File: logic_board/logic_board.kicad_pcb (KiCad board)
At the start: 4 copper layers, 80 x 30 mm, 55 parts, among them J1 Debug, J2 Audio In, J3 SJ2-3595X-SMT, J4 Amphenol 124015, J5 Batt, SW1 TL3315NF160Q, SW2 TL3315NF160Q, SW3 TL3315NF160Q, SW4 TL3315NF160Q, SW5 Power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

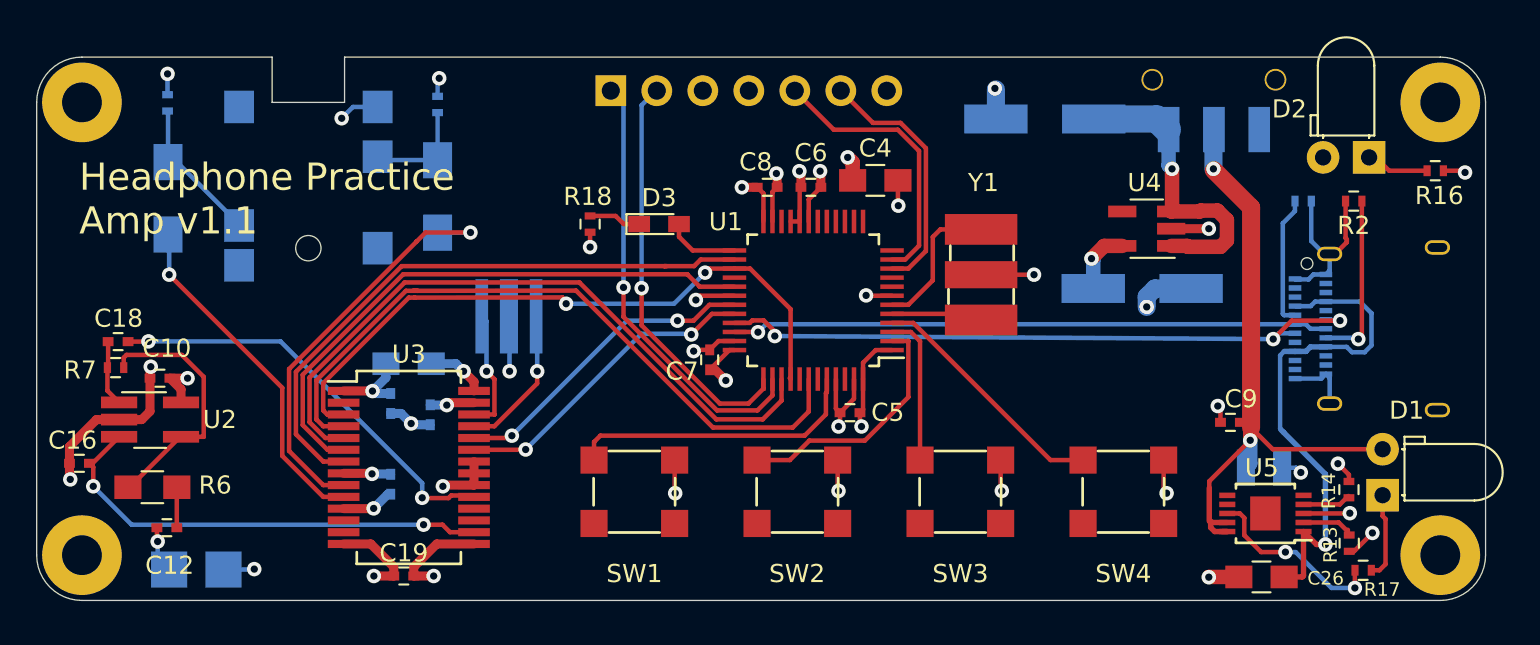
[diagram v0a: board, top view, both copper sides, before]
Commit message: Use longer screws
The M2x6 screws are too short with the PCB in place. This requires upgrading to M2.3 screws.
Increased bore sizes. I had to make the top bosses tapered to accomodate the larger counterbore.
I tapered the bottom ones just to match.
Also increased the RELIEF to 0.8, as the parts do warp a bit and things stick during assembly.
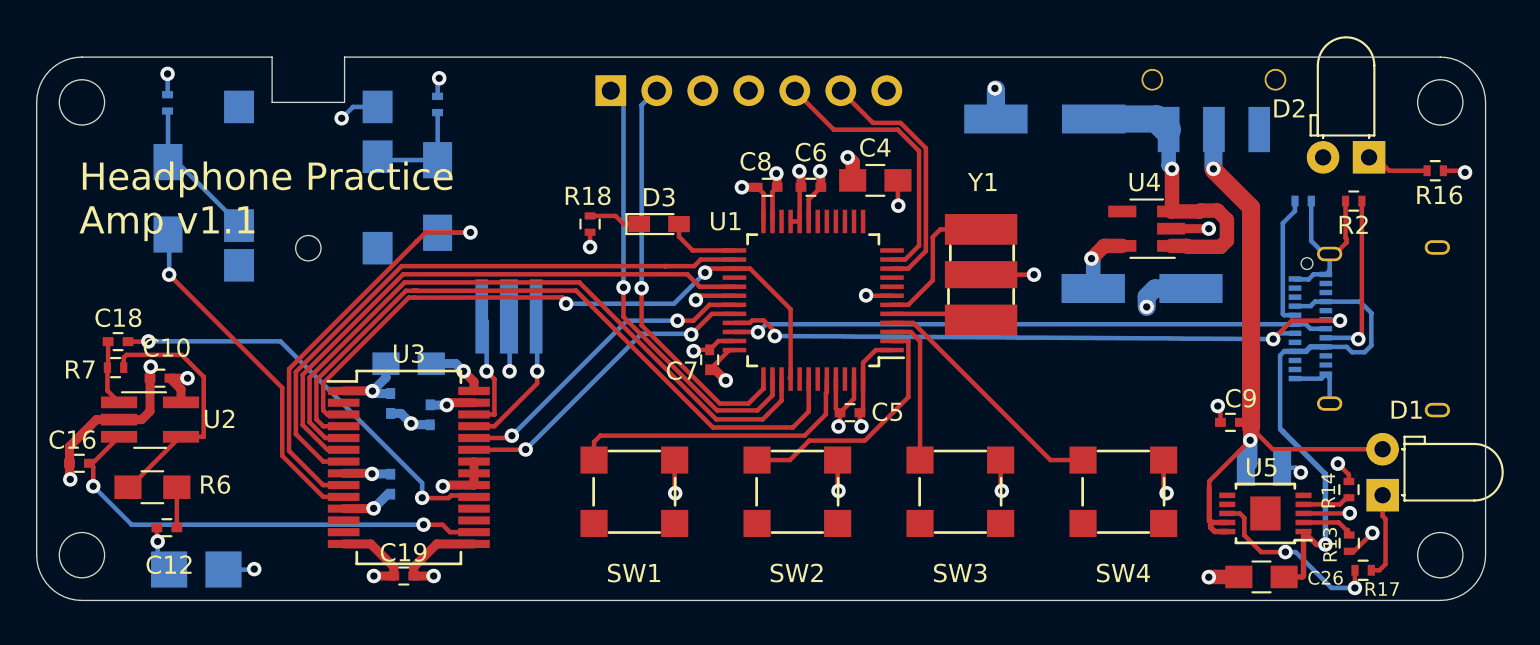
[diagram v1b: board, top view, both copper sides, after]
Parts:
- H1, H2, H3, H4: footprint Mounting_Holes:MountingHole_2.2mm_M2_Pad -> MountingHole:MountingHole_2.5mm
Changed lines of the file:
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@@
     (add_net USB_DP)
+  )
+  (module MountingHole:MountingHole_2.5mm (layer F.Cu)
+    (at 177.5 127.5)
+    (descr "Mounting Hole 2.5mm, no annular")
+    (tags "mounting hole 2.5mm no annular")
+    (attr virtual)
+    (fp_text reference H1 (at 0 -3.2) (layer F.SilkS) hide
+      (effects (font (size 1 1) (thickness 0.15)))
+    )
+    (fp_text value MountingHole (at 0 3.2) (layer F.Fab) hide
+      (effects (font (size 1 1) (thickness 0.15)))
+    )
+    (fp_circle (center 0 0) (end 2.75 0) (layer F.CrtYd) (width 0.05))
+    (fp_circle (center 0 0) (end 2.5 0) (layer Cmts.User) (width 0.15))
+    (fp_text user %R (at 0.3 0) (layer F.Fab)
+      (effects (font (size 1 1) (thickness 0.15)))
+    )
+    (pad 1 np_thru_hole circle (at 0 0) (size 2.5 2.5) (drill 2.5) (layers *.Cu *.Mask))
+  )
+  (module MountingHole:MountingHole_2.5mm (layer F.Cu)
+    (at 177.5 102.5)
+    (descr "Mounting Hole 2.5mm, no annular")
+    (tags "mounting hole 2.5mm no annular")
+    (attr virtual)
+    (fp_text reference H2 (at 0 -3.2) (layer F.SilkS) hide
+      (effects (font (size 1 1) (thickness 0.15)))
+    )
+    (fp_text value MountingHole (at 0 3.2) (layer F.Fab) hide
+      (effects (font (size 1 1) (thickness 0.15)))
+    )
+    (fp_circle (center 0 0) (end 2.75 0) (layer F.CrtYd) (width 0.05))
+    (fp_circle (center 0 0) (end 2.5 0) (layer Cmts.User) (width 0.15))
+    (fp_text user %R (at 0.3 0) (layer F.Fab)
+      (effects (font (size 1 1) (thickness 0.15)))
+    )
+    (pad 1 np_thru_hole circle (at 0 0) (size 2.5 2.5) (drill 2.5) (layers *.Cu *.Mask))
+  )
+  (module MountingHole:MountingHole_2.5mm (layer F.Cu)
+    (at 102.5 127.5)
+    (descr "Mounting Hole 2.5mm, no annular")
+    (tags "mounting hole 2.5mm no annular")
+    (attr virtual)
+    (fp_text reference H3 (at 0 -3.2) (layer F.SilkS) hide
+      (effects (font (size 1 1) (thickness 0.15)))
+    )
+    (fp_text value MountingHole (at 0 3.2) (layer F.Fab) hide
+      (effects (font (size 1 1) (thickness 0.15)))
+    )
+    (fp_circle (center 0 0) (end 2.75 0) (layer F.CrtYd) (width 0.05))
+    (fp_circle (center 0 0) (end 2.5 0) (layer Cmts.User) (width 0.15))
+    (fp_text user %R (at 0.3 0) (layer F.Fab)
+      (effects (font (size 1 1) (thickness 0.15)))
+    )
+    (pad 1 np_thru_hole circle (at 0 0) (size 2.5 2.5) (drill 2.5) (layers *.Cu *.Mask))
+  )
+  (module MountingHole:MountingHole_2.5mm (layer F.Cu)
+    (at 102.5 102.5)
+    (descr "Mounting Hole 2.5mm, no annular")
+    (tags "mounting hole 2.5mm no annular")
+    (attr virtual)
+    (fp_text reference H4 (at 0 -3.2) (layer F.SilkS) hide
+      (effects (font (size 1 1) (thickness 0.15)))
+    )
+    (fp_text value MountingHole (at 0 3.2) (layer F.Fab) hide
+      (effects (font (size 1 1) (thickness 0.15)))
+    )
+    (fp_circle (center 0 0) (end 2.75 0) (layer F.CrtYd) (width 0.05))
+    (fp_circle (center 0 0) (end 2.5 0) (layer Cmts.User) (width 0.15))
+    (fp_text user %R (at 0.3 0) (layer F.Fab)
+      (effects (font (size 1 1) (thickness 0.15)))
+    )
+    (pad 1 np_thru_hole circle (at 0 0) (size 2.5 2.5) (drill 2.5) (layers *.Cu *.Mask))
   )
   (module Pin_Headers:Pin_Header_Straight_1x07_Pitch2.54mm (layer B.Cu)
@@
       (net 2 GND))
   )
-  (module Mounting_Holes:MountingHole_2.2mm_M2_Pad (layer F.Cu)
-    (at 102.5 102.5)
-    (descr "Mounting Hole 2.2mm, M2")
-    (tags "mounting hole 2.2mm m2")
-    (attr virtual)
-    (fp_text reference H4 (at 0 -3.2) (layer F.SilkS) hide
-      (effects (font (size 1 1) (thickness 0.15)))
-    )
-    (fp_text value MountingHole (at 0 3.2) (layer F.Fab) hide
-      (effects (font (size 1 1) (thickness 0.15)))
-    )
-    (fp_text user %R (at 0.3 0) (layer F.Fab)
-      (effects (font (size 1 1) (thickness 0.15)))
-    )
-    (fp_circle (center 0 0) (end 2.2 0) (layer Cmts.User) (width 0.15))
-    (fp_circle (center 0 0) (end 2.45 0) (layer F.CrtYd) (width 0.05))
-    (pad 1 thru_hole circle (at 0 0) (size 4.4 4.4) (drill 2.2) (layers *.Cu *.Mask))
-  )
-  (module Mounting_Holes:MountingHole_2.2mm_M2_Pad (layer F.Cu)
-    (at 102.5 127.5)
-    (descr "Mounting Hole 2.2mm, M2")
-    (tags "mounting hole 2.2mm m2")
-    (attr virtual)
-    (fp_text reference H3 (at 0 -3.2) (layer F.SilkS) hide
-      (effects (font (size 1 1) (thickness 0.15)))
-    )
-    (fp_text value MountingHole (at 0 3.2) (layer F.Fab) hide
-      (effects (font (size 1 1) (thickness 0.15)))
-    )
-    (fp_text user %R (at 0.3 0) (layer F.Fab)
-      (effects (font (size 1 1) (thickness 0.15)))
-    )
-    (fp_circle (center 0 0) (end 2.2 0) (layer Cmts.User) (width 0.15))
-    (fp_circle (center 0 0) (end 2.45 0) (layer F.CrtYd) (width 0.05))
-    (pad 1 thru_hole circle (at 0 0) (size 4.4 4.4) (drill 2.2) (layers *.Cu *.Mask))
-  )
-  (module Mounting_Holes:MountingHole_2.2mm_M2_Pad (layer F.Cu)
-    (at 177.5 102.5)
-    (descr "Mounting Hole 2.2mm, M2")
-    (tags "mounting hole 2.2mm m2")
-    (attr virtual)
-    (fp_text reference H2 (at 0 -3.2) (layer F.SilkS) hide
-      (effects (font (size 1 1) (thickness 0.15)))
-    )
-    (fp_text value MountingHole (at 0 3.2) (layer F.Fab) hide
-      (effects (font (size 1 1) (thickness 0.15)))
-    )
-    (fp_text user %R (at 0.3 0) (layer F.Fab)
-      (effects (font (size 1 1) (thickness 0.15)))
-    )
-    (fp_circle (center 0 0) (end 2.2 0) (layer Cmts.User) (width 0.15))
-    (fp_circle (center 0 0) (end 2.45 0) (layer F.CrtYd) (width 0.05))
-    (pad 1 thru_hole circle (at 0 0) (size 4.4 4.4) (drill 2.2) (layers *.Cu *.Mask))
-  )
-  (module Mounting_Holes:MountingHole_2.2mm_M2_Pad (layer F.Cu)
-    (at 177.5 127.5)
-    (descr "Mounting Hole 2.2mm, M2")
-    (tags "mounting hole 2.2mm m2")
-    (attr virtual)
-    (fp_text reference H1 (at 0 -3.2) (layer F.SilkS) hide
-      (effects (font (size 1 1) (thickness 0.15)))
-    )
-    (fp_text value MountingHole (at 0 3.2) (layer F.Fab) hide
-      (effects (font (size 1 1) (thickness 0.15)))
-    )
-    (fp_text user %R (at 0.3 0) (layer F.Fab)
-      (effects (font (size 1 1) (thickness 0.15)))
-    )
-    (fp_circle (center 0 0) (end 2.2 0) (layer Cmts.User) (width 0.15))
-    (fp_circle (center 0 0) (end 2.45 0) (layer F.CrtYd) (width 0.05))
-    (pad 1 thru_hole circle (at 0 0) (size 4.4 4.4) (drill 2.2) (layers *.Cu *.Mask))
-  )
   (module Capacitors_SMD:C_0805_HandSoldering (layer F.Cu)

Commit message: Nitpicky layout cleanup and alignment
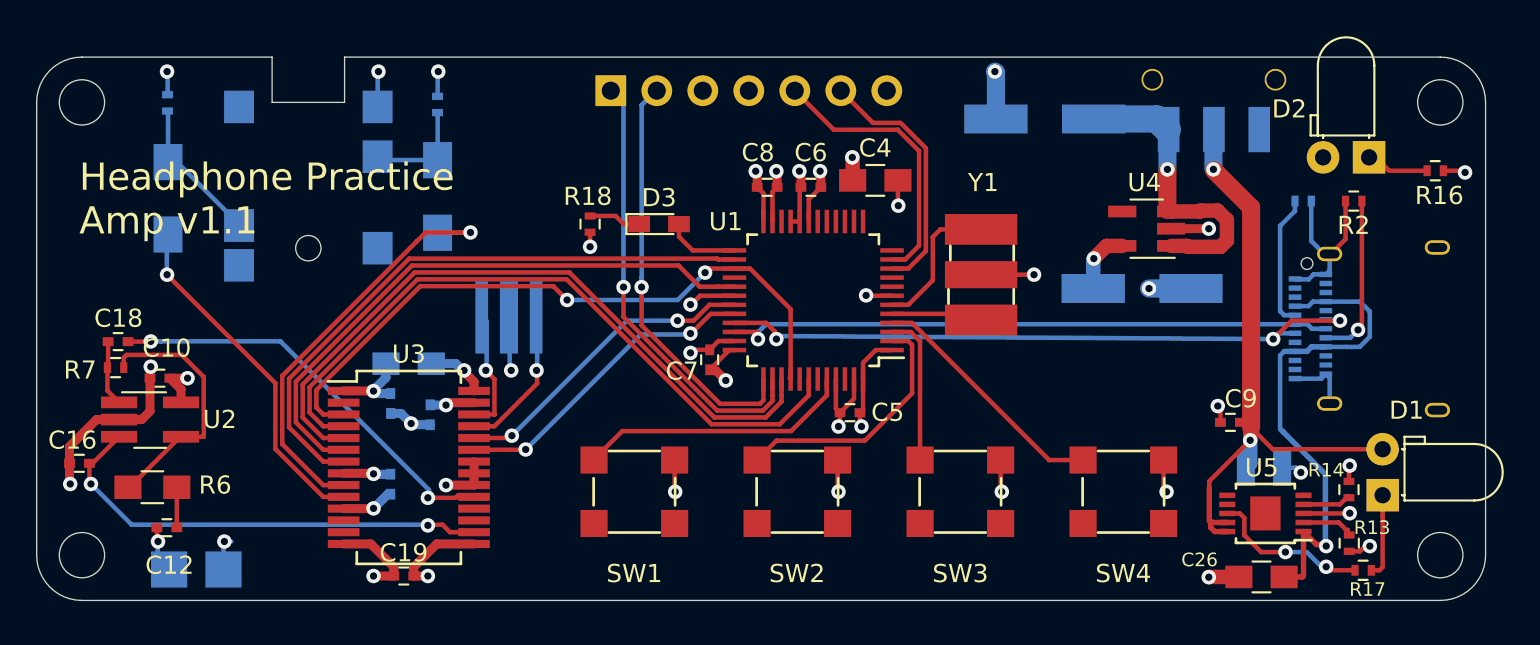
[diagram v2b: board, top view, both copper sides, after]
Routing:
- net Net-(R17-Pad2): track 10.3 -> 8.90 mm
- net SW1: track 16.4 -> 15.3 mm
- net BCLK: track 36.4 -> 37.3 mm
- net ADCDAT: track 32.0 -> 32.9 mm
- net DACLRC: track 37.7 -> 38.5 mm
- net Net-(C26-Pad1): track 28.6 -> 27.9 mm
